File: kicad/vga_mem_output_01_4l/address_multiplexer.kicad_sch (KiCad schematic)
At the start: 7 parts, among them J5 Conn_01x18_Socket, J6 Conn_01x18_Socket, U5 74LS157, U6 74LS157, U7 74LS157, U8 74LS157, U9 74LS157

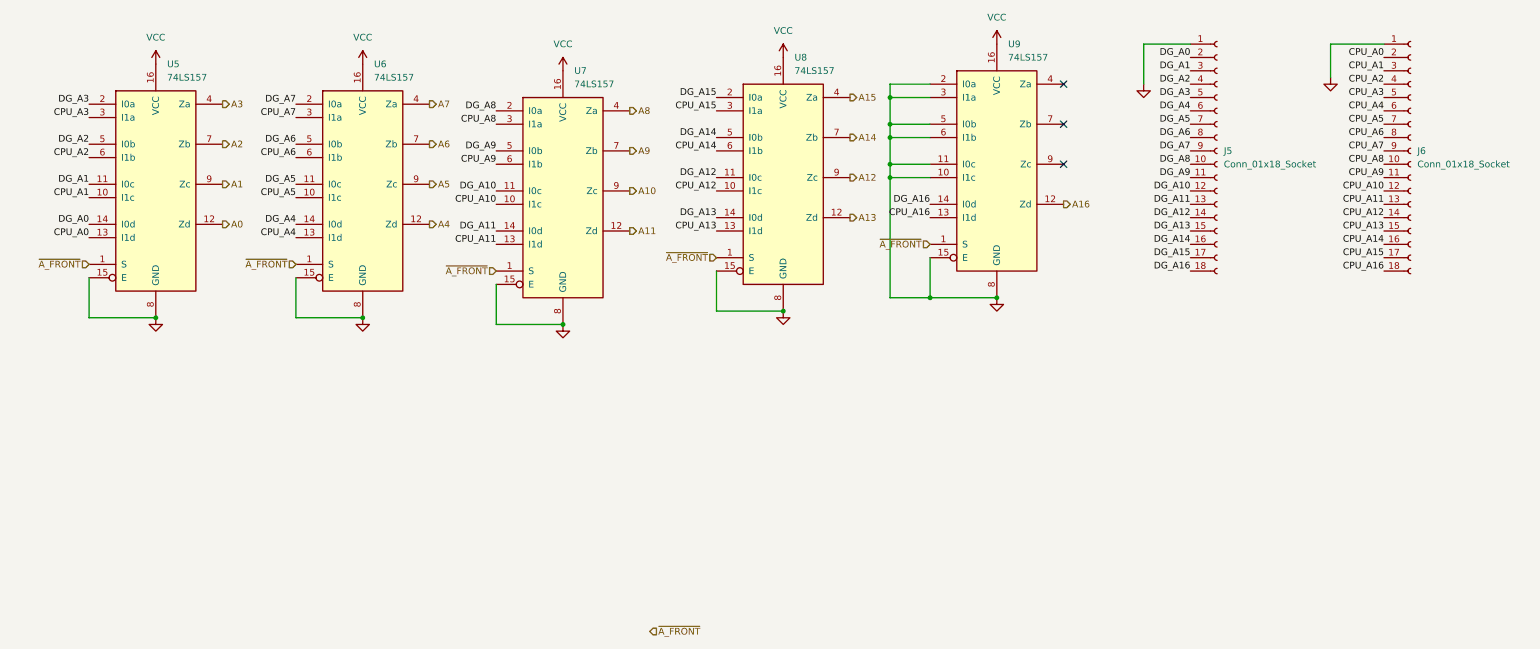
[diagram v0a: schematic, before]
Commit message: added clock circuit ('display generator')
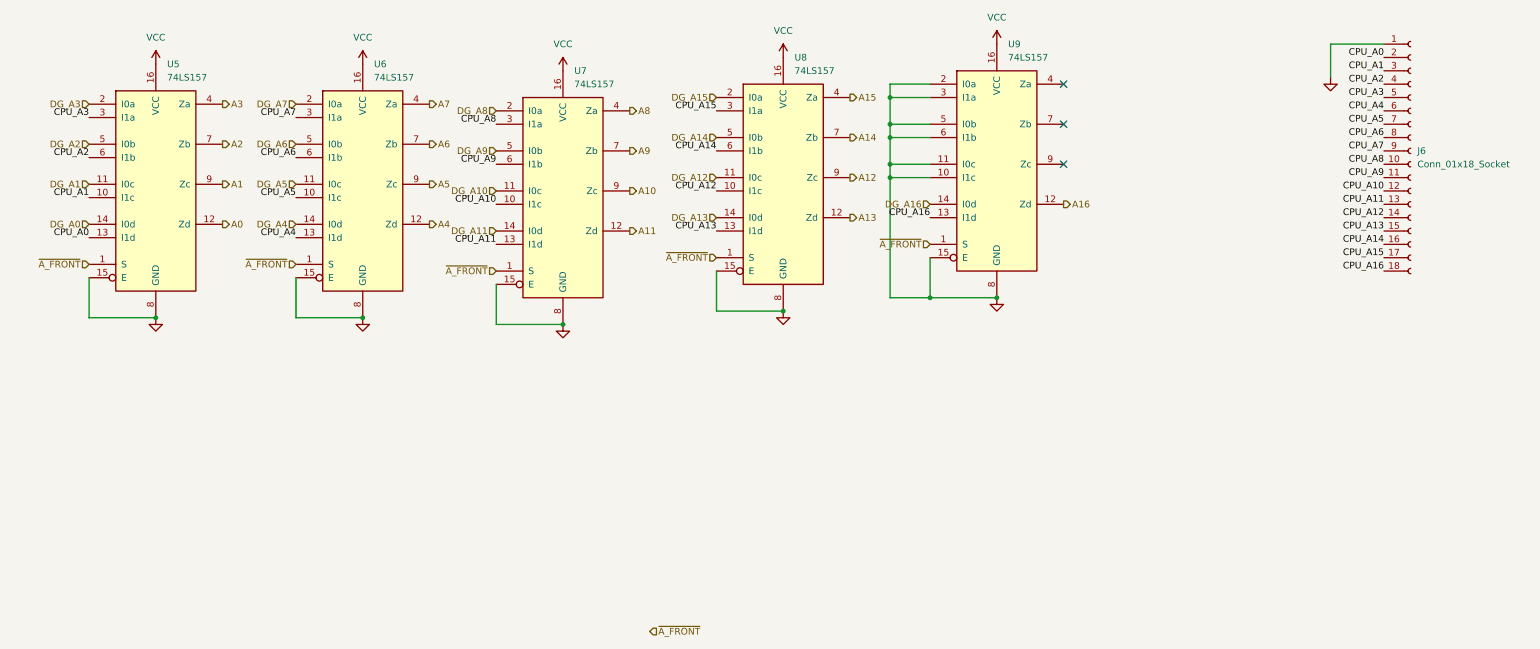
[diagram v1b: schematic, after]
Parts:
- removed J5: Conn_01x18_Socket, Connector_PinHeader_2.54mm:PinHeader_1x18_P2.54mm_Vertical, symbol Connector:Conn_01x18_Socket

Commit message: routing fixes
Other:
- moved on the sheet: J6
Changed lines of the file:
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@@
 	(wire
 		(pts
-			(xy 260.35 34.29) (xy 270.51 34.29)
+			(xy 231.14 36.83) (xy 241.3 36.83)
 		)
 		(stroke
@@
 	(wire
 		(pts
-			(xy 260.35 40.64) (xy 260.35 34.29)
+			(xy 231.14 43.18) (xy 231.14 36.83)
 		)
 		(stroke
@@
 	)
 	(label "CPU_A4"
-		(at 270.51 46.99 180)
+		(at 241.3 49.53 180)
 		(effects
 			(font
@@
 	)
 	(label "CPU_A3"
-		(at 270.51 44.45 180)
+		(at 241.3 46.99 180)
 		(effects
 			(font
@@
 	)
 	(label "CPU_A14"
-		(at 270.51 72.39 180)
+		(at 241.3 74.93 180)
 		(effects
 			(font
@@
 	)
 	(label "CPU_A12"
-		(at 270.51 67.31 180)
+		(at 241.3 69.85 180)
 		(effects
 			(font
@@
 	)
 	(label "CPU_A0"
-		(at 270.51 36.83 180)
+		(at 241.3 39.37 180)
 		(effects
 			(font
@@
 	)
 	(label "CPU_A11"
-		(at 270.51 64.77 180)
+		(at 241.3 67.31 180)
 		(effects
 			(font
@@
 	)
 	(label "CPU_A1"
-		(at 270.51 39.37 180)
+		(at 241.3 41.91 180)
 		(effects
 			(font
@@
 	)
 	(label "CPU_A5"
-		(at 270.51 49.53 180)
+		(at 241.3 52.07 180)
 		(effects
 			(font
@@
 	)
 	(label "CPU_A2"
-		(at 270.51 41.91 180)
+		(at 241.3 44.45 180)
 		(effects
 			(font
@@
 	)
 	(label "CPU_A10"
-		(at 270.51 62.23 180)
+		(at 241.3 64.77 180)
 		(effects
 			(font
@@
 	)
 	(label "CPU_A9"
-		(at 270.51 59.69 180)
+		(at 241.3 62.23 180)
 		(effects
 			(font
@@
 	)
 	(label "CPU_A13"
-		(at 270.51 69.85 180)
+		(at 241.3 72.39 180)
 		(effects
 			(font
@@
 	)
 	(label "CPU_A16"
-		(at 270.51 77.47 180)
+		(at 241.3 80.01 180)
 		(effects
 			(font
@@
 	)
 	(label "CPU_A15"
-		(at 270.51 74.93 180)
+		(at 241.3 77.47 180)
 		(effects
 			(font
@@
 	)
 	(label "CPU_A8"
-		(at 270.51 57.15 180)
+		(at 241.3 59.69 180)
 		(effects
 			(font
@@
 	)
 	(label "CPU_A6"
-		(at 270.51 52.07 180)
+		(at 241.3 54.61 180)
 		(effects
 			(font
@@
 	)
 	(label "CPU_A7"
-		(at 270.51 54.61 180)
+		(at 241.3 57.15 180)
 		(effects
 			(font
@@
 		(shape output)
 		(at 88.9 45.72 0)
-		(effects
-			(font
-				(size 1.27 1.27)
-			)
-			(justify left)
-		)
-	)
-	(hierarchical_label "~{A_FRONT}"
-		(shape input)
-		(at 130.81 146.05 0)
 		(effects
 			(font
@@
 	(symbol
 		(lib_id "power:GND")
-		(at 260.35 40.64 0)
+		(at 231.14 43.18 0)
 		(unit 1)
 		(exclude_from_sim no)
@@
 		(fields_autoplaced yes)
 		(property "Reference" "#PWR053"
-			(at 260.35 46.99 0)
+			(at 231.14 49.53 0)
 			(effects
 				(font
@@
 		)
 		(property "Value" "GND"
-			(at 260.35 45.72 0)
+			(at 231.14 48.26 0)
 			(effects
 				(font
@@
 		)
 		(property "Footprint" ""
-			(at 260.35 40.64 0)
+			(at 231.14 43.18 0)
 			(effects
 				(font
@@
 		)
 		(property "Datasheet" ""
-			(at 260.35 40.64 0)
+			(at 231.14 43.18 0)
 			(effects
 				(font
@@
 		)
 		(property "Description" ""
-			(at 260.35 40.64 0)
+			(at 231.14 43.18 0)
 			(effects
 				(font
@@
 	(symbol
 		(lib_id "Connector:Conn_01x18_Socket")
-		(at 275.59 54.61 0)
+		(at 246.38 57.15 0)
 		(unit 1)
 		(exclude_from_sim no)
@@
 		(fields_autoplaced yes)
 		(property "Reference" "J6"
-			(at 276.86 54.6099 0)
+			(at 247.65 57.1499 0)
 			(effects
 				(font
@@
 		)
 		(property "Value" "Conn_01x18_Socket"
-			(at 276.86 57.1499 0)
+			(at 247.65 59.6899 0)
 			(effects
 				(font
@@
 		)
 		(property "Footprint" "Connector_PinHeader_2.54mm:PinHeader_1x18_P2.54mm_Vertical"
-			(at 275.59 54.61 0)
+			(at 246.38 57.15 0)
 			(effects
 				(font
@@
 		)
 		(property "Datasheet" "~"
-			(at 275.59 54.61 0)
+			(at 246.38 57.15 0)
 			(effects
 				(font
@@
 		)
 		(property "Description" "Generic connector, single row, 01x18, script generated"
-			(at 275.59 54.61 0)
-			(effects
-				(font
+			(at 246.38 57.15 0)
+			(effects
+				(font

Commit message: switch to VCC pour on signal layers, revised signal / ref assignments
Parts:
- J6: footprint Connector_PinHeader_2.54mm:PinHeader_1x18_P2.54mm_Vertical -> Connector_PinHeader_2.54mm:PinHeader_1x19_P2.54mm_Vertical; symbol Connector:Conn_01x18_Socket -> Connector:Conn_01x19_Socket
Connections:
- net GND: now also J6.19 (Pin_19)
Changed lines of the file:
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@@
+	)
+	(junction
+		(at 231.14 82.55)
+		(diameter 0)
+		(color 0 0 0 0)
 	)
 	(junction
@@
 	(wire
 		(pts
+			(xy 231.14 82.55) (xy 231.14 36.83)
+		)
+		(stroke
+			(width 0)
+			(type default)
+		)
+	)
+	(wire
+		(pts
 			(xy 143.51 77.47) (xy 143.51 85.09)
 		)
@@
 	(wire
 		(pts
-			(xy 231.14 43.18) (xy 231.14 36.83)
+			(xy 231.14 87.63) (xy 231.14 82.55)
 		)
 		(stroke
@@
 		(pts
 			(xy 176.53 44.45) (xy 176.53 41.91)
+		)
+		(stroke
+			(width 0)
+			(type default)
+		)
+	)
+	(wire
+		(pts
+			(xy 231.14 82.55) (xy 241.3 82.55)
 		)
 		(stroke
@@
 	(symbol
 		(lib_id "power:GND")
-		(at 231.14 43.18 0)
+		(at 231.14 87.63 0)
 		(unit 1)
 		(exclude_from_sim no)
@@
 		(fields_autoplaced yes)
 		(property "Reference" "#PWR053"
-			(at 231.14 49.53 0)
+			(at 231.14 93.98 0)
 			(effects
 				(font
@@
 		)
 		(property "Value" "GND"
-			(at 231.14 48.26 0)
+			(at 231.14 92.71 0)
 			(effects
 				(font
@@
 		)
 		(property "Footprint" ""
-			(at 231.14 43.18 0)
+			(at 231.14 87.63 0)
 			(effects
 				(font
@@
 		)
 		(property "Datasheet" ""
-			(at 231.14 43.18 0)
+			(at 231.14 87.63 0)
 			(effects
 				(font
@@
 		)
 		(property "Description" ""
-			(at 231.14 43.18 0)
+			(at 231.14 87.63 0)
 			(effects
 				(font
@@
 	)
 	(symbol
-		(lib_id "Connector:Conn_01x18_Socket")
-		(at 246.38 57.15 0)
+		(lib_id "Connector:Conn_01x19_Socket")
+		(at 246.38 59.69 0)
 		(unit 1)
 		(exclude_from_sim no)
@@
 		(fields_autoplaced yes)
 		(property "Reference" "J6"
-			(at 247.65 57.1499 0)
+			(at 247.65 58.4199 0)
 			(effects
 				(font
@@
 		)
 		(property "Value" "Conn_01x18_Socket"
-			(at 247.65 59.6899 0)
+			(at 247.65 60.9599 0)
 			(effects
 				(font
@@
 			)
 		)
-		(property "Footprint" "Connector_PinHeader_2.54mm:PinHeader_1x18_P2.54mm_Vertical"
-			(at 246.38 57.15 0)
+		(property "Footprint" "Connector_PinHeader_2.54mm:PinHeader_1x19_P2.54mm_Vertical"
+			(at 246.38 59.69 0)
 			(effects
 				(font
@@
 		)
 		(property "Datasheet" "~"
-			(at 246.38 57.15 0)
-			(effects
-				(font
-					(size 1.27 1.27)
-				)
-				(hide yes)
-			)
-		)
-		(property "Description" "Generic connector, single row, 01x18, script generated"
-			(at 246.38 57.15 0)
+			(at 246.38 59.69 0)
+			(effects
+				(font
+					(size 1.27 1.27)
+				)
+				(hide yes)
+			)
+		)
+		(property "Description" "Generic connector, single row, 01x19, script generated"
+			(at 246.38 59.69 0)
 			(effects
 				(font
@@
 		(pin "4"
 		)
+		(pin "19"
+		)
 		(instances
